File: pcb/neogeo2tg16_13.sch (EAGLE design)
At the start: 8 parts, among them IC5 74HC157N

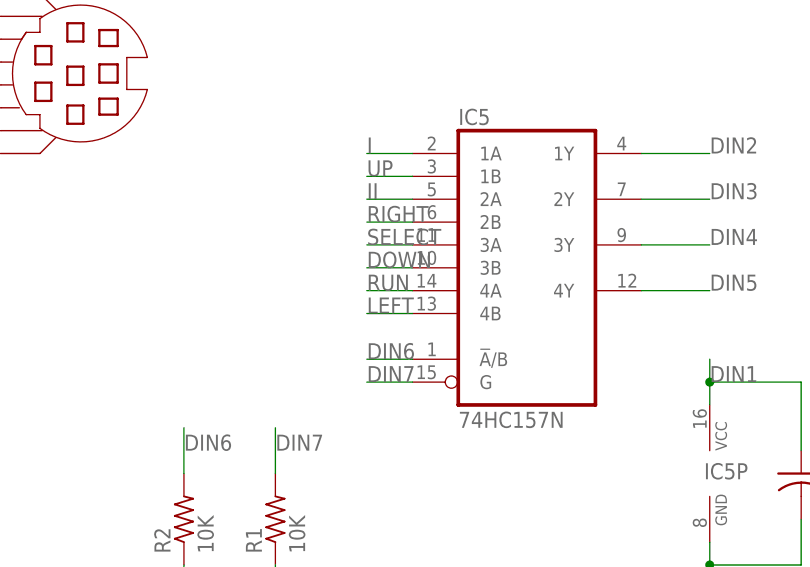
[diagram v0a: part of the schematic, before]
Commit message: Fixed start button not working in the NeoGeo to TG16 adapter
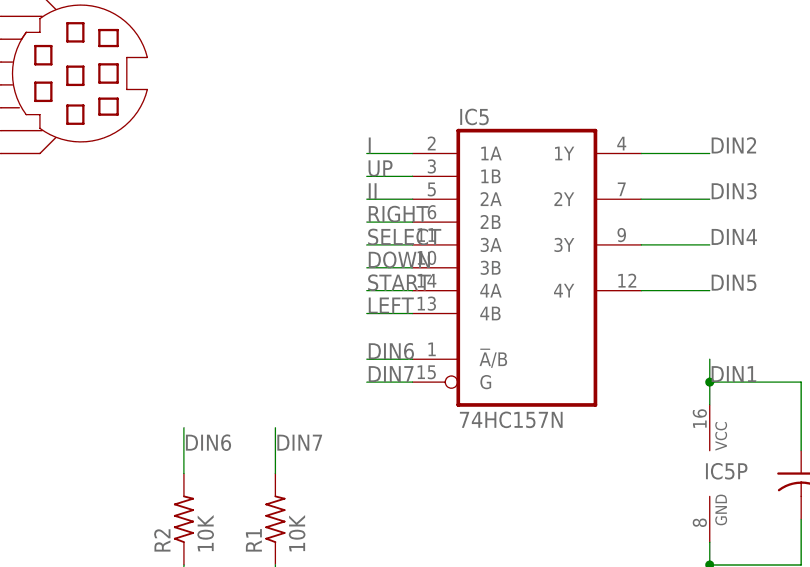
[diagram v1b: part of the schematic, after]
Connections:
- removed net RUN: IC5A.4A
- net START: now also IC5A.4A
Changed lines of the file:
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@@
-</segment>
-</net>
-<net name="RUN" class="0">
-<segment>
-<pinref part="IC5" gate="A" pin="4A"/>
-<wire x1="127" y1="22.86" x2="121.92" y2="22.86" width="0.1524" layer="91"/>
-<label x="121.92" y="22.86" size="1.778" layer="95"/>
 </segment>
 </net>
@@
 <label x="40.64" y="-12.7" size="1.778" layer="95"/>
 </segment>
+<segment>
+<pinref part="IC5" gate="A" pin="4A"/>
+<wire x1="127" y1="22.86" x2="121.92" y2="22.86" width="0.1524" layer="91"/>
+<label x="121.92" y="22.86" size="1.778" layer="95"/>
+</segment>
 </net>
